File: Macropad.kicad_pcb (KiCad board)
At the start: 2 copper layers, 59.9 x 119.9 mm, 56 parts, among them SW1 SW_Push, SW10 SW_Push, SW11 SW_Push, SW12 SW_Push, SW2 SW_Push, SW3 SW_Push, SW4 SW_Push, SW5 SW_Push, SW6 SW_Push, SW7 SW_Push, SW8 SW_Push, SW9 SW_Push

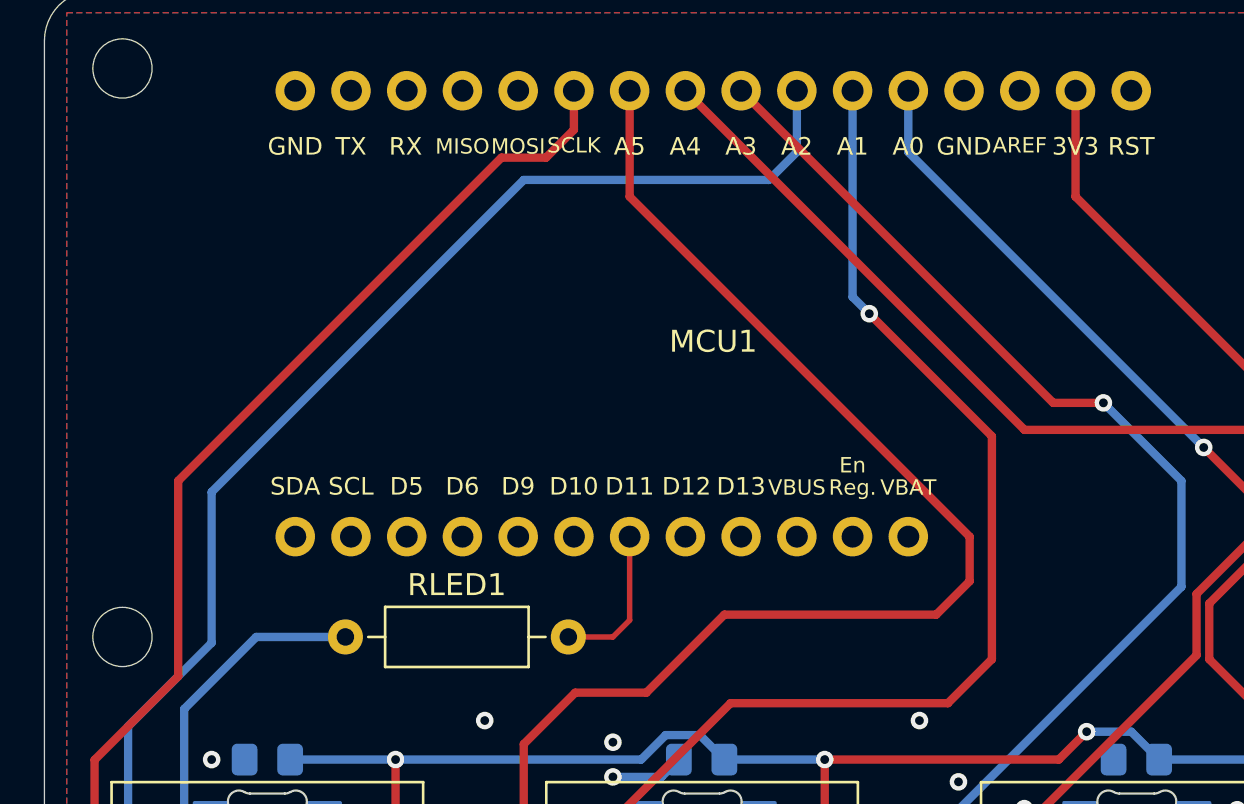
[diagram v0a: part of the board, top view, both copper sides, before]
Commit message: Added silkscreen stuff
Signed-off-by: Kozova1 <mug66kk@gmail.com>
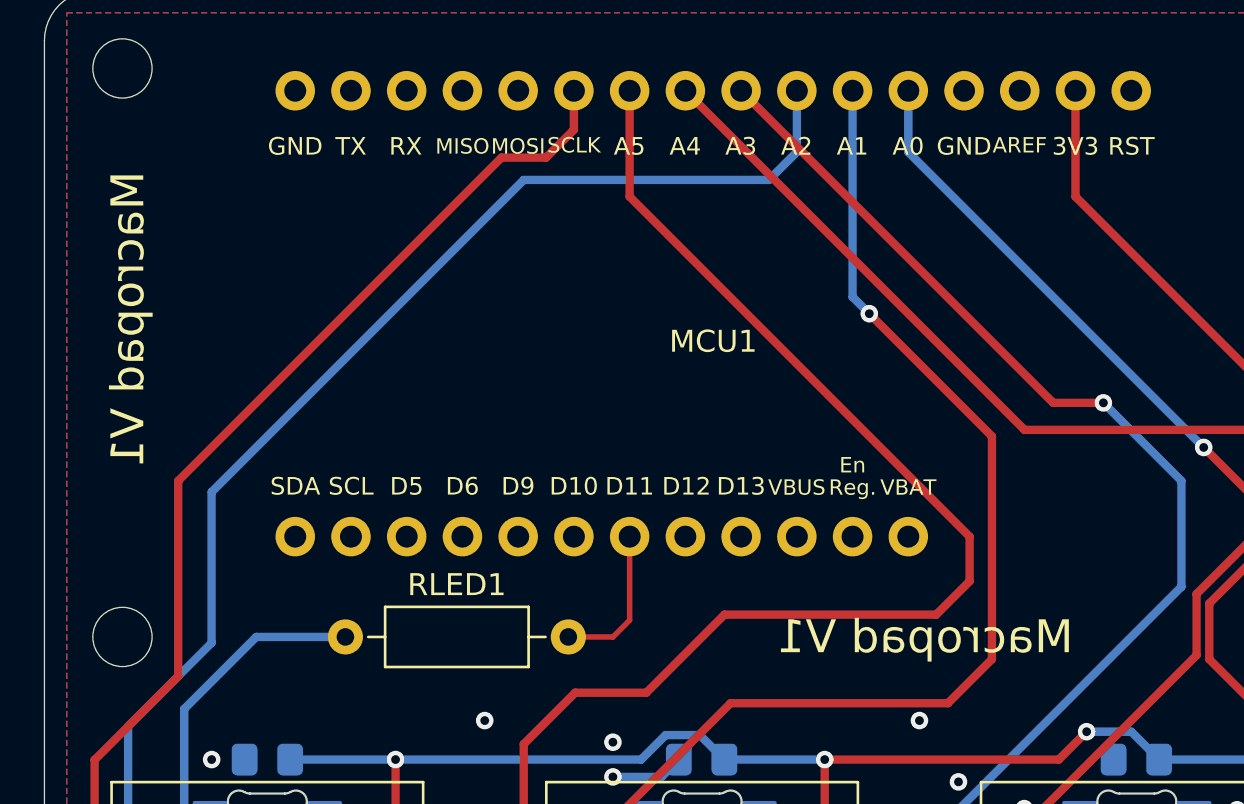
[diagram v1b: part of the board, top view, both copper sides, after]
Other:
- board text added: "Macropad V1"
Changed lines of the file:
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@@
-(kicad_pcb (version 20210722) (generator pcbnew)
+(kicad_pcb (version 20210824) (generator pcbnew)
   (general
     (thickness 1.6)
@@
     (fp_circle (center 0 0) (end 2.7 0) (layer "Cmts.User") (width 0.15) (fill none))
     (fp_circle (center 0 0) (end 2.95 0) (layer "F.CrtYd") (width 0.05) (fill none))
-    (pad "1" np_thru_hole circle locked (at 0 0) (size 2.7 2.7) (drill 2.7) (layers *.Cu *.Mask))
+    (pad "" np_thru_hole circle locked (at 0 0) (size 2.7 2.7) (drill 2.7) (layers *.Cu *.Mask))
   )
   (footprint "MountingHole:MountingHole_2.7mm_M2.5" (layer "F.Cu")
@@
     (fp_circle (center 0 0) (end 2.7 0) (layer "Cmts.User") (width 0.15) (fill none))
     (fp_circle (center 0 0) (end 2.95 0) (layer "F.CrtYd") (width 0.05) (fill none))
-    (pad "1" np_thru_hole circle locked (at 0 0) (size 2.7 2.7) (drill 2.7) (layers *.Cu *.Mask))
+    (pad "" np_thru_hole circle locked (at 0 0) (size 2.7 2.7) (drill 2.7) (layers *.Cu *.Mask))
   )
   (footprint "MountingHole:MountingHole_2.7mm_M2.5" (layer "F.Cu")
@@
     (fp_circle (center 0 0) (end 2.7 0) (layer "Cmts.User") (width 0.15) (fill none))
     (fp_circle (center 0 0) (end 2.95 0) (layer "F.CrtYd") (width 0.05) (fill none))
-    (pad "1" np_thru_hole circle locked (at 0 0) (size 2.7 2.7) (drill 2.7) (layers *.Cu *.Mask))
+    (pad "" np_thru_hole circle locked (at 0 0) (size 2.7 2.7) (drill 2.7) (layers *.Cu *.Mask))
   )
   (footprint "MountingHole:MountingHole_2.7mm_M2.5" (layer "F.Cu")
@@
     (fp_circle (center 0 0) (end 2.7 0) (layer "Cmts.User") (width 0.15) (fill none))
     (fp_circle (center 0 0) (end 2.95 0) (layer "F.CrtYd") (width 0.05) (fill none))
-    (pad "1" np_thru_hole circle locked (at 0 0) (size 2.7 2.7) (drill 2.7) (layers *.Cu *.Mask))
+    (pad "" np_thru_hole circle locked (at 0 0) (size 2.7 2.7) (drill 2.7) (layers *.Cu *.Mask))
   )
   (footprint "MountingHole:MountingHole_2.7mm_M2.5" (layer "F.Cu")
@@
     (fp_circle (center 0 0) (end 2.7 0) (layer "Cmts.User") (width 0.15) (fill none))
     (fp_circle (center 0 0) (end 2.95 0) (layer "F.CrtYd") (width 0.05) (fill none))
-    (pad "1" np_thru_hole circle locked (at 0 0) (size 2.7 2.7) (drill 2.7) (layers *.Cu *.Mask))
+    (pad "" np_thru_hole circle locked (at 0 0) (size 2.7 2.7) (drill 2.7) (layers *.Cu *.Mask))
   )
   (footprint "AdafruitFeather:Adafruit_Feather_conn.kicad_mod" (layer "F.Cu")
@@
     (fp_circle (center 0 0) (end 2.7 0) (layer "Cmts.User") (width 0.15) (fill none))
     (fp_circle (center 0 0) (end 2.95 0) (layer "F.CrtYd") (width 0.05) (fill none))
-    (pad "1" np_thru_hole circle locked (at 0 0) (size 2.7 2.7) (drill 2.7) (layers *.Cu *.Mask))
+    (pad "" np_thru_hole circle locked (at 0 0) (size 2.7 2.7) (drill 2.7) (layers *.Cu *.Mask))
   )
   (footprint "Capacitor_SMD:C_0805_2012Metric_Pad1.18x1.45mm_HandSolder" (layer "B.Cu")
@@
   (gr_arc (start 81.026 25.654) (end 81.026 23.368) (angle -90) (layer "Edge.Cuts") (width 0.05))
   (gr_arc (start 136.398 25.654) (end 138.684 25.654) (angle -90) (layer "Edge.Cuts") (width 0.05))
+  (gr_text "Macropad V1" (at 82.55 38.354 90) (layer "F.SilkS")
+    (effects (font (size 1.5 1.5) (thickness 0.3)) (justify mirror))
+  )
+  (gr_text "Macropad V1" (at 118.872 52.832) (layer "F.SilkS")
+    (effects (font (size 1.5 1.5) (thickness 0.3)) (justify mirror))
+  )
   (segment (start 111.76 76.2) (end 111.223499 75.663499) (width 0.381) (layer "F.Cu") (net 1))
   (segment (start 131.035499 75.663499) (end 117.884501 75.663499) (width 0.381) (layer "F.Cu") (net 1))
